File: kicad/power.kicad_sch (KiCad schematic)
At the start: 29 parts, among them Q1 CSD17576Q5B, Q2 CSD17308Q3, Q6 BSS138, Q9 BSS138, U1 TPS40305

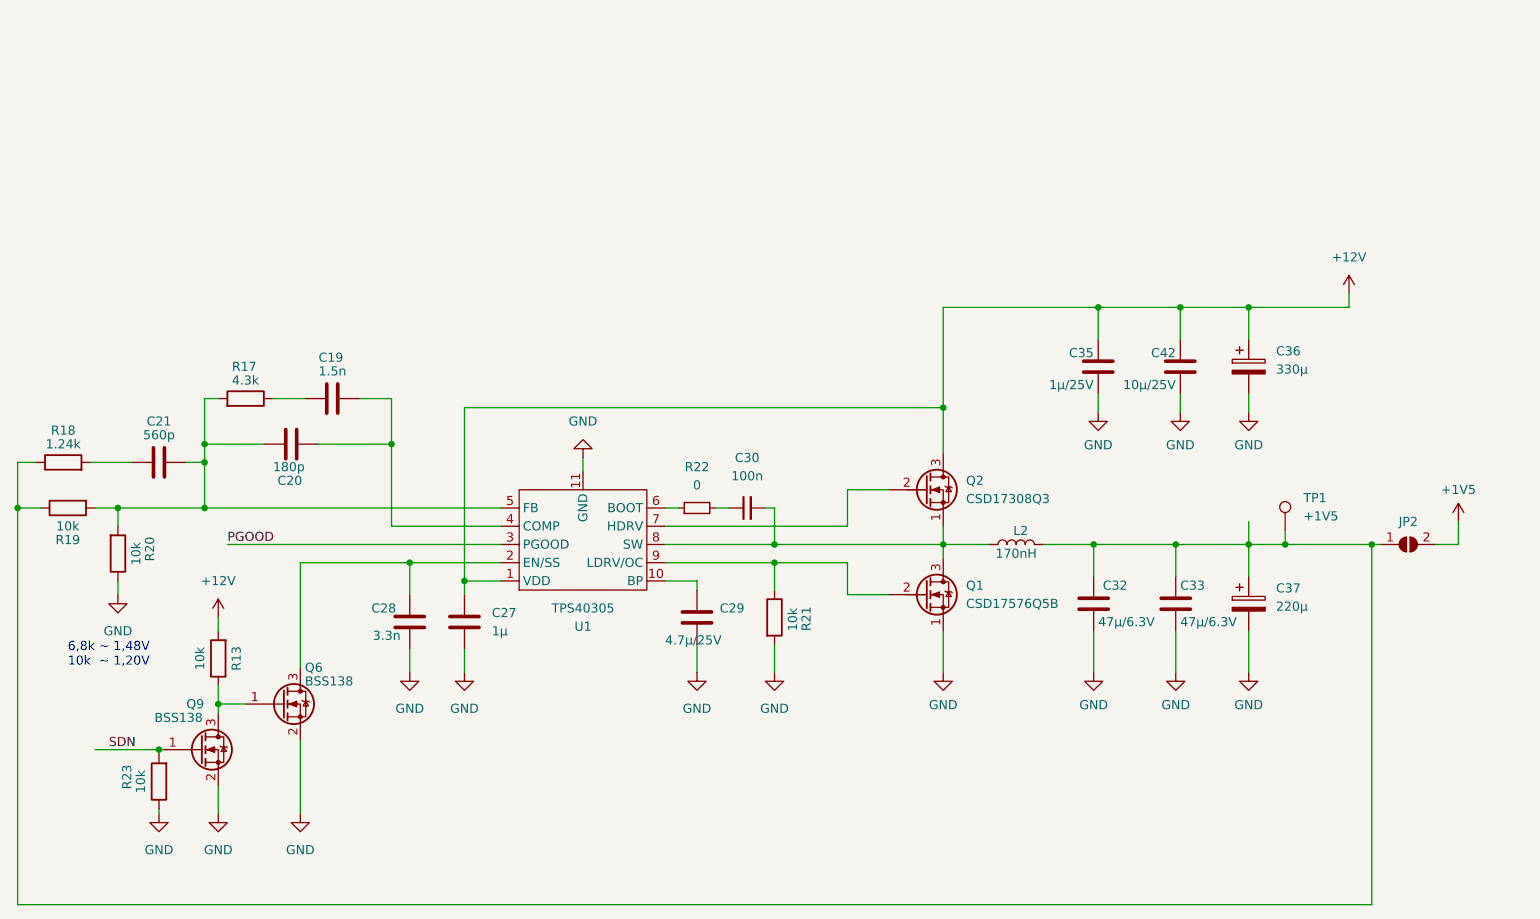
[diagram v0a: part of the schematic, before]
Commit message: added solderjumper to enable the buck without Pi, changed LED values to 560R
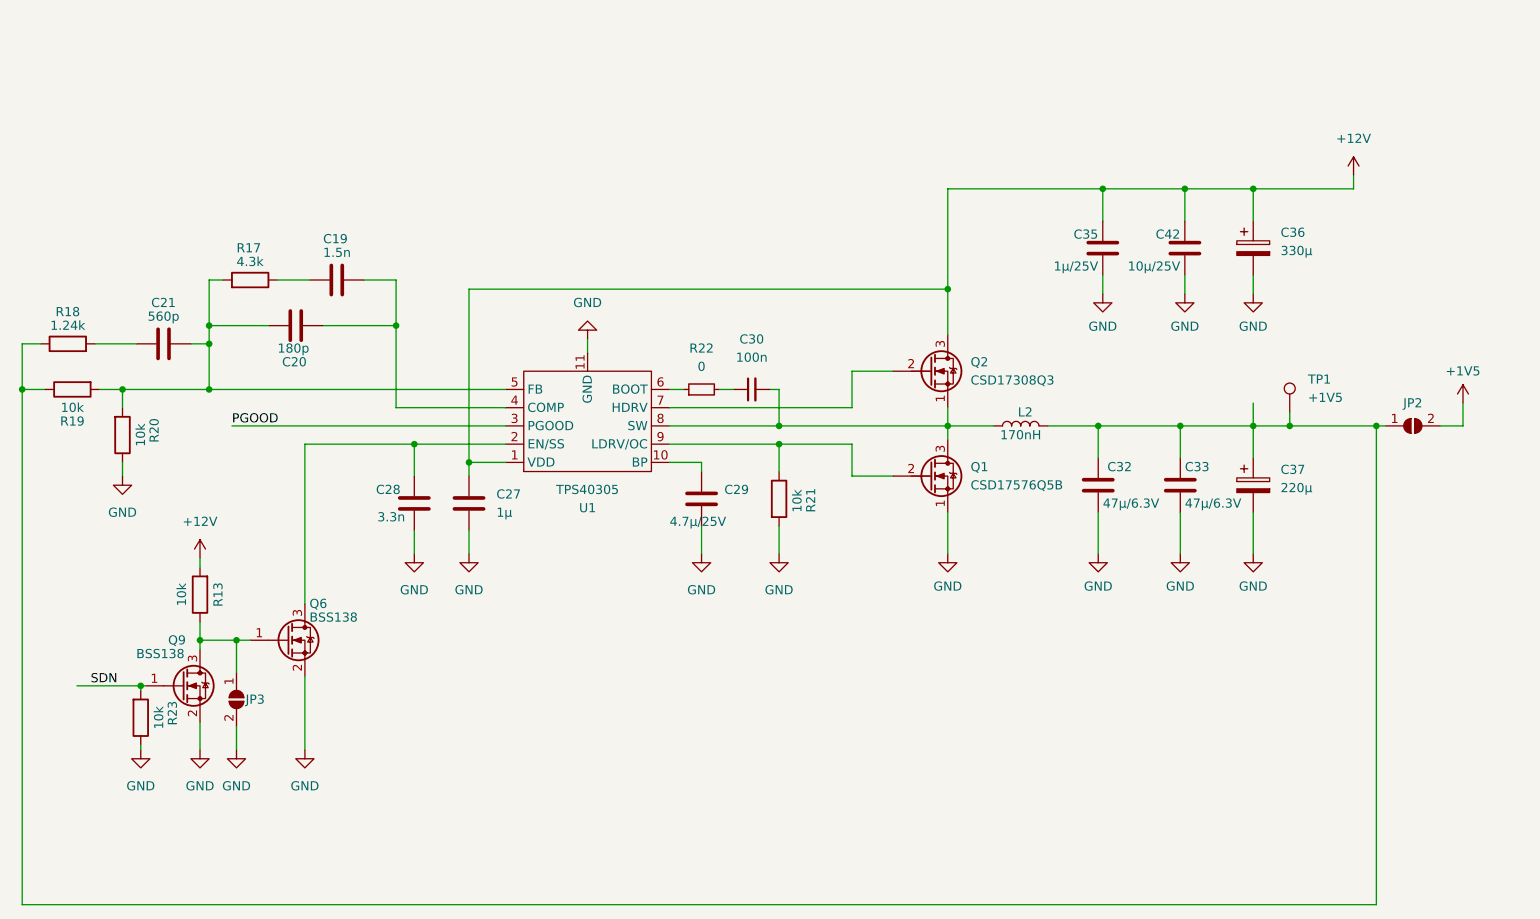
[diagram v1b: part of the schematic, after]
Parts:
- added JP3: SolderJumper_2_Open, Jumper:SolderJumper-2_P1.3mm_Open_RoundedPad1.0x1.5mm, symbol Jumper:SolderJumper_2_Open
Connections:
- net GND: now also JP3.2 (B)
- net at Q6.1 (G), Q9.3 (D), R13.1: now also JP3.1 (A)
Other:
- note removed: "6,8k ~ 1,48V 10k ~ 1,20V"
- moved on the sheet: C19, C20, C21, C27, C28, C29, C30, C32, C33, C35, C36, C37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

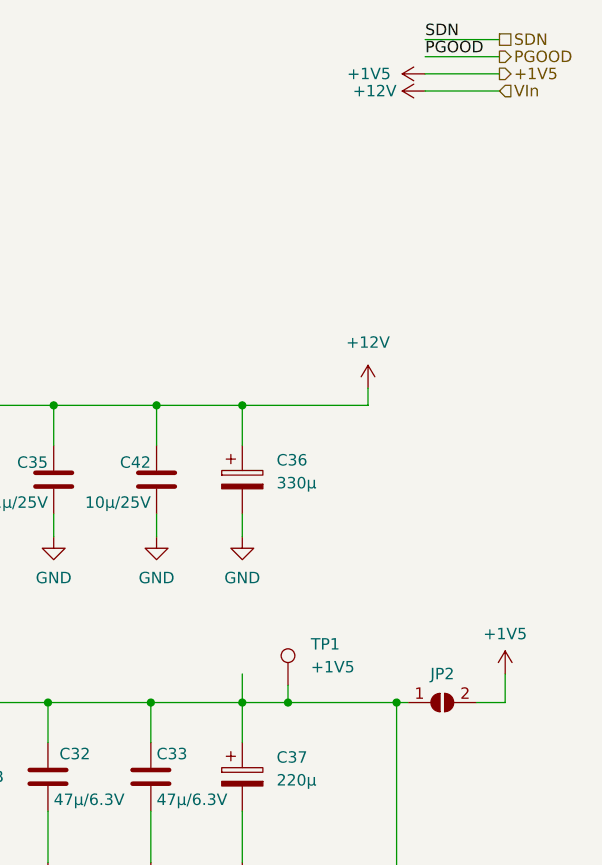
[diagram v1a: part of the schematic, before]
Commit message: fixed net labeling to 1.2V
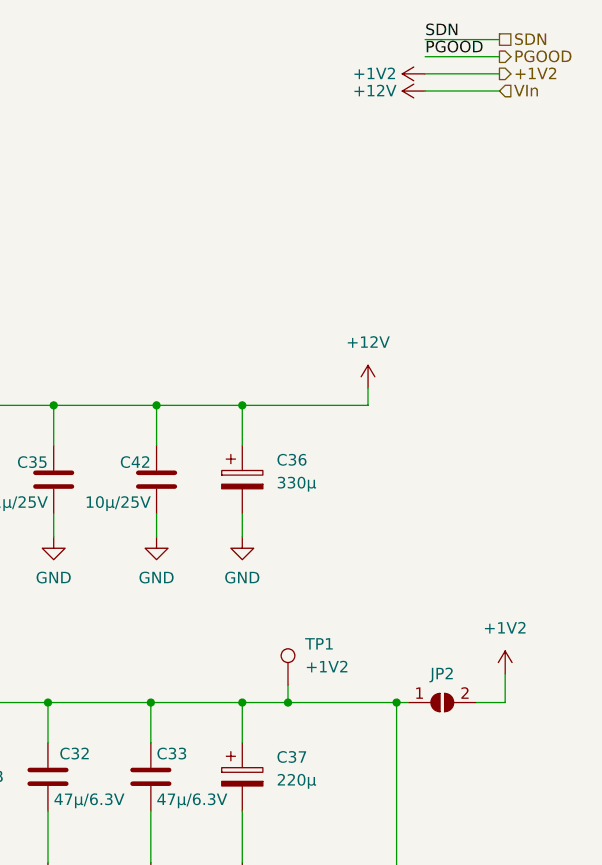
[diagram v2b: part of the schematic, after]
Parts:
- TP1: value +1V5 -> +1V2
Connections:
- net +1V5 renamed +1V2
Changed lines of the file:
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@@
-    (stroke (width 0) (type default))
-  )
-  (wire (pts (xy 222.885 96.52) (xy 222.885 99.695))
     (stroke (width 0) (type default))
   )
@@
     (effects (font (size 1.27 1.27)) (justify left bottom))
   )
-  (hierarchical_label "+1V5" (shape output) (at 251.46 29.845 0) (fields_autoplaced)
+  (hierarchical_label "+1V2" (shape output) (at 251.46 29.845 0) (fields_autoplaced)
     (effects (font (size 1.27 1.27)) (justify left))
   )
@@
   (symbol (lib_id "Connector:TestPoint") (at 227.965 97.79 0) (unit 1)
     (in_bom yes) (on_board yes) (dnp no) (fields_autoplaced)
-    (property "Reference" "TP1" (at 230.505 93.218 0)
-      (effects (font (size 1.27 1.27)) (justify left))
-    )
-    (property "Value" "+1V5" (at 230.505 95.758 0)
+    (property "Reference" "TP1" (at 229.87 93.218 0)
+      (effects (font (size 1.27 1.27)) (justify left))
+    )
+    (property "Value" "+1V2" (at 229.87 95.758 0)
       (effects (font (size 1.27 1.27)) (justify left))
     )
@@
         (path "/e63e39d7-6ac0-4ffd-8aa3-1841a4541b55/8ec0a9c6-2b78-44ef-a83d-9047d2828409"
           (reference "#PWR083") (unit 1)
+        )
+      )
+    )
+  )
+  (symbol (lib_id "power:+1V2") (at 243.205 29.845 90) (unit 1)
+    (in_bom yes) (on_board yes) (dnp no) (fields_autoplaced)
+    (property "Reference" "#PWR05" (at 247.015 29.845 0)
+      (effects (font (size 1.27 1.27)) hide)
+    )
+    (property "Value" "+1V2" (at 240.03 29.845 90)
+      (effects (font (size 1.27 1.27)) (justify left))
+    )
+    (property "Footprint" "" (at 243.205 29.845 0)
+      (effects (font (size 1.27 1.27)) hide)
+    )
+    (property "Datasheet" "" (at 243.205 29.845 0)
+      (effects (font (size 1.27 1.27)) hide)
+    )
+    (pin "1")
+    (instances
+      (project "piaxe"
+        (path "/e63e39d7-6ac0-4ffd-8aa3-1841a4541b55/8ec0a9c6-2b78-44ef-a83d-9047d2828409"
+          (reference "#PWR05") (unit 1)
         )
       )
@@
     )
   )
-  (symbol (lib_id "power:+1V5") (at 243.205 29.845 90) (unit 1)
-    (in_bom yes) (on_board yes) (dnp no) (fields_autoplaced)
-    (property "Reference" "#PWR018" (at 247.015 29.845 0)
-      (effects (font (size 1.27 1.27)) hide)
-    )
-    (property "Value" "+1V5" (at 239.395 29.845 90)
-      (effects (font (size 1.27 1.27)) (justify left))
-    )
-    (property "Footprint" "" (at 243.205 29.845 0)
-      (effects (font (size 1.27 1.27)) hide)
-    )
-    (property "Datasheet" "" (at 243.205 29.845 0)
-      (effects (font (size 1.27 1.27)) hide)
-    )
-    (pin "1")
-    (instances
-      (project "piaxe"
-        (path "/e63e39d7-6ac0-4ffd-8aa3-1841a4541b55/8ec0a9c6-2b78-44ef-a83d-9047d2828409"
-          (reference "#PWR018") (unit 1)
-        )
-      )
-    )
-  )
   (symbol (lib_id "power:GND") (at 67.945 144.78 0) (unit 1)
     (in_bom yes) (on_board yes) (dnp no) (fields_autoplaced)
@@
     )
   )
-  (symbol (lib_id "power:+1V5") (at 252.095 96.52 0) (unit 1)
-    (in_bom yes) (on_board yes) (dnp no) (fields_autoplaced)
-    (property "Reference" "#PWR05" (at 252.095 100.33 0)
-      (effects (font (size 1.27 1.27)) hide)
-    )
-    (property "Value" "+1V5" (at 252.095 92.075 0)
+  (symbol (lib_id "power:GND") (at 130.175 87.63 180) (unit 1)
+    (in_bom yes) (on_board yes) (dnp no) (fields_autoplaced)
+    (property "Reference" "#PWR071" (at 130.175 81.28 0)
+      (effects (font (size 1.27 1.27)) hide)
+    )
+    (property "Value" "GND" (at 130.175 82.55 0)
+      (effects (font (size 1.27 1.27)))
+    )
+    (property "Footprint" "" (at 130.175 87.63 0)
+      (effects (font (size 1.27 1.27)) hide)
+    )
+    (property "Datasheet" "" (at 130.175 87.63 0)
+      (effects (font (size 1.27 1.27)) hide)
+    )
+    (pin "1")
+    (instances
+      (project "piaxe"
+        (path "/e63e39d7-6ac0-4ffd-8aa3-1841a4541b55/8ec0a9c6-2b78-44ef-a83d-9047d2828409"
+          (reference "#PWR071") (unit 1)
+        )
+      )
+    )
+  )
+  (symbol (lib_id "power:+1V2") (at 252.095 96.52 0) (unit 1)
+    (in_bom yes) (on_board yes) (dnp no) (fields_autoplaced)
+    (property "Reference" "#PWR0120" (at 252.095 100.33 0)
+      (effects (font (size 1.27 1.27)) hide)
+    )
+    (property "Value" "+1V2" (at 252.095 91.44 0)
       (effects (font (size 1.27 1.27)))
     )
@@
       (project "piaxe"
         (path "/e63e39d7-6ac0-4ffd-8aa3-1841a4541b55/8ec0a9c6-2b78-44ef-a83d-9047d2828409"
-          (reference "#PWR05") (unit 1)
-        )
-      )
-    )
-  )
-  (symbol (lib_id "power:GND") (at 130.175 87.63 180) (unit 1)
-    (in_bom yes) (on_board yes) (dnp no) (fields_autoplaced)
-    (property "Reference" "#PWR071" (at 130.175 81.28 0)
-      (effects (font (size 1.27 1.27)) hide)
-    )
-    (property "Value" "GND" (at 130.175 82.55 0)
-      (effects (font (size 1.27 1.27)))
-    )
-    (property "Footprint" "" (at 130.175 87.63 0)
-      (effects (font (size 1.27 1.27)) hide)
-    )
-    (property "Datasheet" "" (at 130.175 87.63 0)
-      (effects (font (size 1.27 1.27)) hide)
-    )
-    (pin "1")
-    (instances
-      (project "piaxe"
-        (path "/e63e39d7-6ac0-4ffd-8aa3-1841a4541b55/8ec0a9c6-2b78-44ef-a83d-9047d2828409"
-          (reference "#PWR071") (unit 1)
-        )
-      )
+          (reference "#PWR0120") (unit 1)
+        )
+      )

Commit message: initial commit before replacing power supply
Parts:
- removed C19: 1.5n, Capacitor_SMD:C_0805_2012Metric, symbol Device:C
- removed C20: 180p, Capacitor_SMD:C_0805_2012Metric, symbol Device:C
- removed C21: 560p, Capacitor_SMD:C_0805_2012Metric, symbol Device:C
- removed C27: 1µ, Capacitor_SMD:C_0805_2012Metric, symbol Device:C
- removed C28: 3.3n, Capacitor_SMD:C_0805_2012Metric, symbol Device:C
- removed C29: 4.7µ/25V, Capacitor_SMD:C_0805_2012Metric, symbol Device:C
- removed C30: 100n, Capacitor_SMD:C_0805_2012Metric, symbol Device:C_Small
- removed C32, C33: 47µ/6.3V, Capacitor_SMD:C_1210_3225Metric, symbol Device:C
- removed C35: 1µ/25V, Capacitor_SMD:C_1210_3225Metric, symbol Device:C
- removed C36: 330µ, Capacitor_SMD:CP_Elec_8x10, symbol Device:C_Polarized
- removed C37: 220µ, Capacitor_SMD:CP_Elec_5x5.8, symbol Device:C_Polarized
- removed C42: 10µ/25V, Capacitor_SMD:C_1210_3225Metric, symbol Device:C
- removed JP2: SolderJumper_2_Open, myfootprints:SolderJumper1.0x4.5, symbol Jumper:SolderJumper_2_Open
- removed JP3: SolderJumper_2_Open, Jumper:SolderJumper-2_P1.3mm_Open_RoundedPad1.0x1.5mm, symbol Jumper:SolderJumper_2_Open
- removed L2: 170nH, myfootprints:IFLR-4031GC-01-8x10, symbol Device:L
- removed Q1: CSD17576Q5B, Package_SON:VSONP-8-1EP_5x6_P1.27mm, symbol Device:Q_NMOS_SGD
- removed Q2: CSD17308Q3, Package_SON:VSONP-8-1EP_5x6_P1.27mm, symbol Device:Q_NMOS_SGD
- removed Q6, Q9: BSS138, Package_TO_SOT_SMD:SOT-23, symbol Transistor_FET:BSS138
- removed R13, R19, R20, R21: 10k, Resistor_SMD:R_0805_2012Metric, symbol Device:R
- removed R17: 4.3k, Resistor_SMD:R_0805_2012Metric, symbol Device:R
- removed R18: 1.24k, Resistor_SMD:R_0805_2012Metric, symbol Device:R
- removed R22: 0, Resistor_SMD:R_1206_3216Metric, symbol Device:R_Small
- removed TP1: +1V2, TestPoint:TestPoint_Pad_D2.0mm, symbol Connector:TestPoint
- removed U1: TPS40305, Package_SON:VSON-10-1EP_3x3mm_P0.5mm_EP1.65x2.4mm_ThermalVias, symbol mylib7:TPS40304
- added C15: 10n/250V, Capacitor_SMD:C_0805_2012Metric, symbol Device:C_Small
- added C22, C23, C65, C66: 100n, Capacitor_SMD:C_0805_2012Metric, symbol Device:C
- added C24: 22µ/16V, Capacitor_SMD:C_1206_3216Metric, symbol Device:C
- added C24, C25: 1µ, Capacitor_SMD:C_0805_2012Metric, symbol Device:C
- added C50, C51: 1n, Capacitor_SMD:C_0805_2012Metric, symbol Device:C_Small
- added C52, C53: 100n, Capacitor_SMD:C_0805_2012Metric, symbol Device:C_Small
- added C54: 4.7µ, Capacitor_SMD:C_0805_2012Metric, symbol Device:C_Small
- added C55, C56, C58, C59: 100µ/6.3V, Capacitor_SMD:C_1210_3225Metric, symbol Device:C
- added C57, C60: 330µ, Capacitor_SMD:CP_Elec_5x5.8, symbol Device:C_Polarized
- added C61, C62: 220µ, Capacitor_SMD:CP_Elec_5x5.8, symbol Device:C_Polarized
- added C63: 3.3n, Capacitor_SMD:C_0805_2012Metric, symbol Device:C
- added C64: 47p, Capacitor_SMD:C_0805_2012Metric, symbol Device:C
- added C9: 10µF/50V, Capacitor_SMD:C_1206_3216Metric, symbol Device:C
- added D4, D5: D_Schottky_Small, Diode_SMD:D_SOD-323, symbol Device:D_Schottky_Small
- added D9: PMEG4030EP,115, Diode_SMD:D_SOD-128, symbol Device:D_Schottky
- added L1: 4.7µH/2A/3A, Inductor_SMD:L_Taiyo-Yuden_NR-50xx, symbol Device:L
- added L1, L3: 220nH, myfootprints:IFLR-4031GC-01-8x10, symbol Device:L
- added NT1 (x3), NT2, NT3, NT4: NetTie_2, NetTie:NetTie-2_SMD_Pad0.5mm, symbol Device:NetTie_2
- added Q3, Q4, Q7, Q8: CSD17308Q3, Package_SON:VSONP-8-1EP_5x6_P1.27mm, symbol Device:Q_NMOS_SGD
- added R16, R24: 10, Resistor_SMD:R_0805_2012Metric, symbol Device:R
- added R2, R29, R3, R30: 200, Resistor_SMD:R_0805_2012Metric, symbol Device:R
- added R24: 49,9k, Resistor_SMD:R_0805_2012Metric, symbol Device:R
- added R25: 16.3k, Resistor_SMD:R_0805_2012Metric, symbol Device:R
- added R25: 100k, Resistor_SMD:R_0805_2012Metric, symbol Device:R
- added R26: 0, Resistor_SMD:R_1210_3225Metric, symbol Device:R
- added R26, R27: 20k, Resistor_SMD:R_0805_2012Metric, symbol Device:R
- added R28: 8.45k, Resistor_SMD:R_0805_2012Metric, symbol Device:R
- added R31: 2.2R, Resistor_SMD:R_2010_5025Metric, symbol Device:R
- added R5, R7: 0.001, Resistor_SMD:R_2010_5025Metric, symbol Device:R
- added TP2: 3V3, TestPoint:TestPoint_Pad_2.0x2.0mm, symbol Connector:TestPoint
- added U17: LTC3856, Package_DFN_QFN:QFN-32-1EP_5x5mm_P0.5mm_EP3.45x3.45mm_ThermalVias, symbol mylib7:LTC3856_reduced
- added U3: AP3211, Package_TO_SOT_SMD:SOT-23-6, symbol pferdibank-rescue:AP3211-mylib
- added U4 (x2): +0V8, symbol mylib7:+0V8
- added U5: MCP1824T-1802E, Package_TO_SOT_SMD:SOT-23-5, symbol bitaxe:MCP1824
- added U6: MCP1824T-0802E, Package_TO_SOT_SMD:SOT-23-5, symbol bitaxe:MCP1824
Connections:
- net +12V: now also C61.1, C62.1, C9.1, Q3.3 (D), Q7.3 (D), R31.1, U3.4 (EN), U3.5 (IN)
- net +1V2: now also C55.1, C56.1, C57.1, C58.1, C59.1, C60.1, NT1.2, NT1.2, NT3.1, R5.2, R7.2
- net GND: now also C22.2, C23.2, C24.2, C24.2, C25.2, C54.2, C55.2, C56.2, C57.2, C58.2, C59.2, C60.2, C61.2, C62.2, C64.2, C65.2, C66.1, C9.2, D9.2 (A), NT1.2, Q4.1 (S), Q8.1 (S), R25.1, R25.2, R27.2, R28.2, U17.33 (SGND), U3.2 (GND), U5.2 (GND), U6.2 (GND)
- net SDN: no longer R23.2
- new net: C51.1, R2.1, U17.7 (SENSE2+)
- new net: NT1.1, R24.1
- new net: C15.1, U3.1 (BS)
- new net: C15.2, D9.1 (K), L1.1, U3.6 (SW)
- new net: C53.2, L3.1, Q7.1 (S), Q8.3 (D), U17.16 (SW2)
- new net: L3.2, NT2.2, R5.1
- new net: C63.2, R28.1
- new net: C50.2, R30.2, U17.31 (SENSE1+)
- new net: C66.2, R31.2, U17.22 (VIN)
- new net: C24.1, L1.2, R24.1, R26.1, TP2.1
- new net: NT1.1, R16.1
- new net: R24.2, R25.1, U3.3 (FB)
- new net: Q4.2 (G), U17.23 (BG1)
- new net: C52.1, L1.1, Q3.1 (S), Q4.3 (D), U17.26 (SW1)
- new net: L1.2, NT4.1, R7.1
- new net: Q3.2 (G), U17.25 (TG1)
- new net: C54.1, D4.2 (A), D5.2 (A), U17.21 (INTVCC)
- new net: C65.1, U17.1 (TK/SS)
- new net: R26.1, U17.11 (DIFFOUT)
- new net: Q7.2 (G), U17.17 (TG2)
- new net: C53.1, D5.1 (K), U17.18 (BOOST2)
- new net: Q8.2 (G), U17.19 (BG2)
- new net: R26.2, R27.1, U17.2 (VFB)
- new net: C52.2, D4.1 (K), U17.24 (BOOST1)
- new net: R25.2, U17.29 (FREQ)
- new net: C63.1, C64.1, U17.3 (ITH)
- new net: C50.1, R29.1, U17.32 (SENSE1-)
- new net: C51.2, R3.1, U17.8 (SENSE2-)
- new net +0V8: C25.1, U4.1 (+0V8), U4.1 (+0V8), U6.5 (VOUT)
- new net +1V8: C24.1, U5.5 (VOUT)
- new net +3V3: C22.1, C23.1, R26.2, U5.1 (VIN), U5.3 (EN), U6.1 (VIN), U6.3 (EN)
- new net 1V2_PGOOD: U17.15 (PGOOD)
- new net 1V2_RUN: R23.2, U17.30 (RUN)
- new net DIFF+: R24.2, U17.9 (DIFFP)
- new net DIFF-: R16.2, U17.10 (DIFFN)
- new net SENSE1+: NT4.2, R30.1
- new net SENSE1-: NT3.2, R29.2
- new net SENSE2+: NT2.1, R2.2
- new net SENSE2-: NT1.1, R3.2
- no-connect marks 0 -> 3
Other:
- moved on the sheet: R23
